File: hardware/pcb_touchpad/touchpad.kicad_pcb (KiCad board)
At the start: 2 copper layers, 23 parts

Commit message: drew outline of trackpad
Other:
- board outline added: 41.3 x 30.3 mm

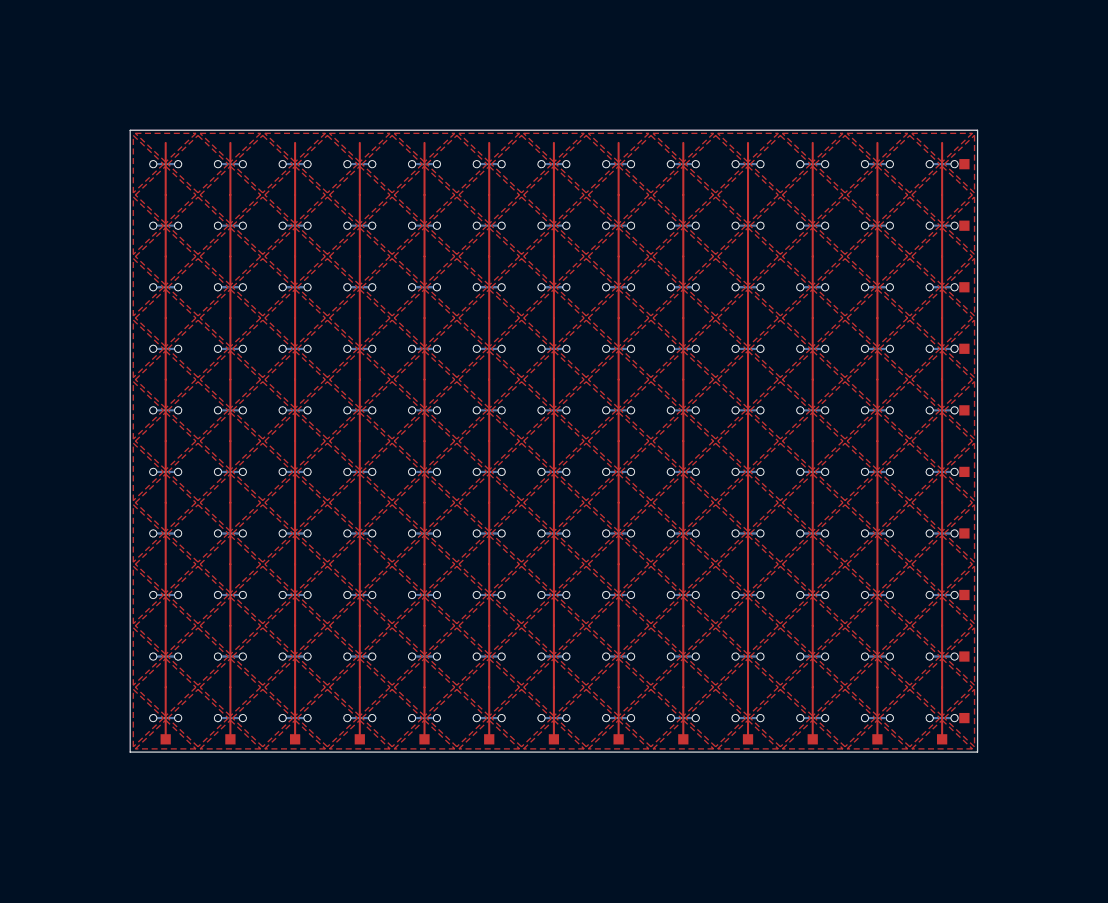
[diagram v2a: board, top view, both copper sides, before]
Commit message: modified QFN footprint of IQS9151
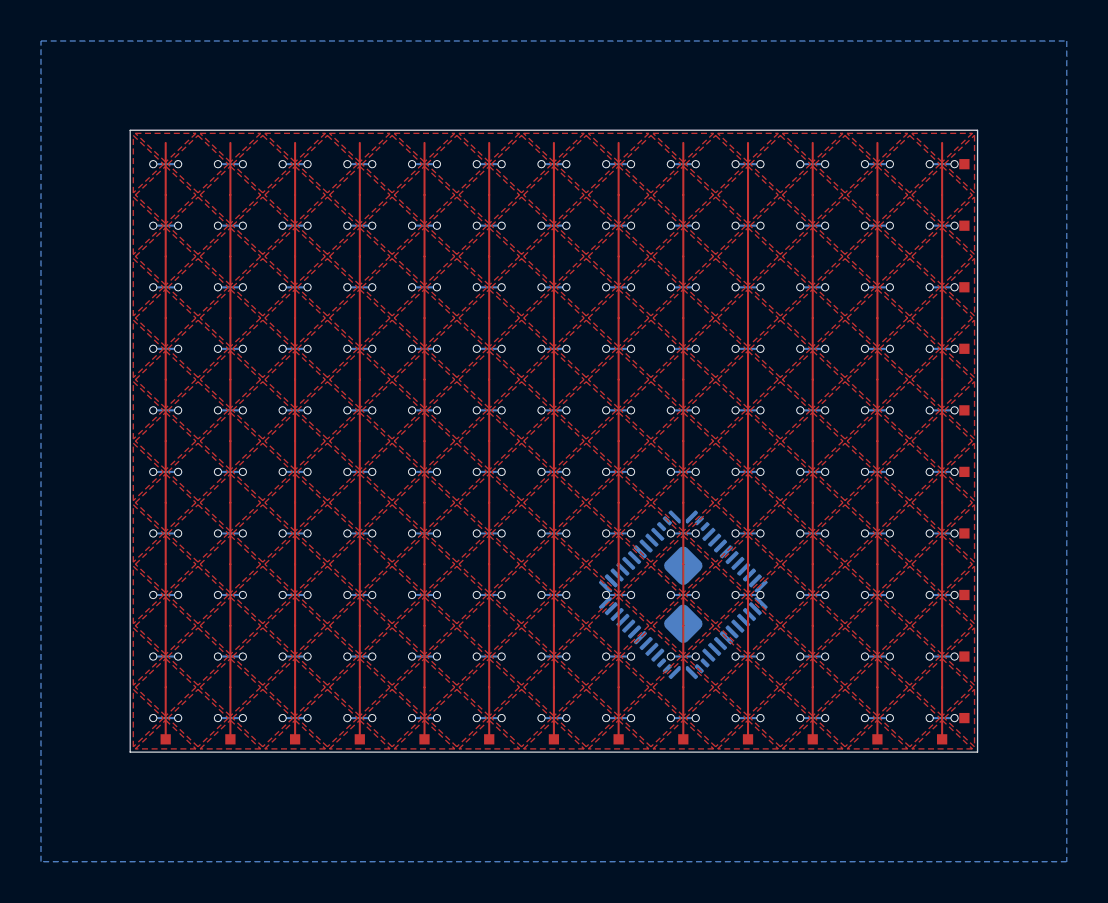
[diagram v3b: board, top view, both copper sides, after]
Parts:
- added U1: IQS9151, Package_DFN_QFN:VQFN-52-1EP_6x6mm_P0.4mm_EP4.7x4.7mm, B.Cu at (169.8, 92.0)
- COL1, COL10, COL2, COL3, COL4, COL5, COL6, COL7, COL8, COL9, ROW1, ROW10, ROW11, ROW12, ROW13, ROW2, ROW3, ROW4, ROW5, ROW6, ROW7, ROW8, ROW9: value (none) -> TESTPOINTPAD_0_5MM
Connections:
- COL1 pad P1: COL1 -> Net-(U1-RX9/TX9)
- COL10 pad P1: COL10 -> Net-(U1-RX0/TX0)
- COL2 pad P1: COL2 -> Net-(U1-RX8/TX8)
- COL3 pad P1: COL3 -> Net-(U1-RX7/TX7)
- COL4 pad P1: COL4 -> Net-(U1-RX6/TX6)
- COL5 pad P1: COL5 -> Net-(U1-RX5/TX5)
- COL6 pad P1: COL6 -> Net-(U1-RX4/TX4)
- COL7 pad P1: COL7 -> Net-(U1-RX3/TX3)
- COL8 pad P1: COL8 -> Net-(U1-RX2/TX2)
- COL9 pad P1: COL9 -> Net-(U1-RX1/TX1)
- ROW1 pad P1: ROW1 -> Net-(U1-TX43)
- ROW10 pad P1: ROW10 -> Net-(U1-TX34)
- ROW11 pad P1: ROW11 -> Net-(U1-TX33)
- ROW12 pad P1: ROW12 -> Net-(U1-RX12/TX12)
- ROW13 pad P1: ROW13 -> Net-(U1-RX11/TX11)
- ROW2 pad P1: ROW2 -> Net-(U1-TX42)
- ROW3 pad P1: ROW3 -> Net-(U1-TX41)
- ROW4 pad P1: ROW4 -> Net-(U1-TX40)
- ROW5 pad P1: ROW5 -> Net-(U1-TX39)
- ROW6 pad P1: ROW6 -> Net-(U1-TX38)
- ROW7 pad P1: ROW7 -> Net-(U1-TX37)
- ROW8 pad P1: ROW8 -> Net-(U1-TX36)
- ROW9 pad P1: ROW9 -> Net-(U1-TX35)
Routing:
- net (no net): track 0.00 -> 141.8 mm, vias 0 -> 234
- net Net-(U1-TX33): track 0.00 -> 31.5 mm, vias 0 -> 4
- net Net-(U1-TX40): track 0.00 -> 30.3 mm, vias 0 -> 2
- net ROW5: track 29.1 -> 0.00 mm
- net Net-(U1-TX39): track 0.00 -> 29.1 mm
- net ROW12: track 29.1 -> 0.00 mm
- net ROW10: track 29.1 -> 0.00 mm
- net Net-(U1-TX34): track 0.00 -> 29.1 mm
- net Net-(U1-RX12/TX12): track 0.00 -> 29.1 mm
- net ROW9: track 29.1 -> 0.00 mm
- net ROW7: track 29.1 -> 0.00 mm
- net ROW11: track 29.1 -> 0.00 mm
- net Net-(U1-TX37): track 0.00 -> 29.1 mm
- net Net-(U1-TX35): track 0.00 -> 29.1 mm
- net ROW8: track 29.1 -> 0.00 mm
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- added copper zone on B.Cu, net GND
- added copper zone on F.Cu, net Net-(U1-RX0/TX0)
- added copper zone on F.Cu, net Net-(U1-RX11/TX11)
- added copper zone on F.Cu, net Net-(U1-RX12/TX12)
- added copper zone on F.Cu, net Net-(U1-RX1/TX1)
- added copper zone on F.Cu, net Net-(U1-RX2/TX2)
- added copper zone on F.Cu, net Net-(U1-RX3/TX3)
- added copper zone on F.Cu, net Net-(U1-RX4/TX4)
- added copper zone on F.Cu, net Net-(U1-RX5/TX5)
- added copper zone on F.Cu, net Net-(U1-RX6/TX6)
- added copper zone on F.Cu, net Net-(U1-RX7/TX7)
- added copper zone on F.Cu, net Net-(U1-RX8/TX8)
- added copper zone on F.Cu, net Net-(U1-RX9/TX9)
- added copper zone on F.Cu, net Net-(U1-TX33)
- added copper zone on F.Cu, net Net-(U1-TX34)
- added copper zone on F.Cu, net Net-(U1-TX35)
- added copper zone on F.Cu, net Net-(U1-TX36)
- added copper zone on F.Cu, net Net-(U1-TX37)
- added copper zone on F.Cu, net Net-(U1-TX38)
- added copper zone on F.Cu, net Net-(U1-TX39)
- added copper zone on F.Cu, net Net-(U1-TX40)
- added copper zone on F.Cu, net Net-(U1-TX41)
- added copper zone on F.Cu, net Net-(U1-TX42)
- added copper zone on F.Cu, net Net-(U1-TX43)
- removed copper zone on F.Cu, net COL1
- removed copper zone on F.Cu, net COL10
- removed copper zone on F.Cu, net COL2
- removed copper zone on F.Cu, net COL3
- removed copper zone on F.Cu, net COL4
- removed copper zone on F.Cu, net COL5
- removed copper zone on F.Cu, net COL6
- removed copper zone on F.Cu, net COL7
- removed copper zone on F.Cu, net COL8
- removed copper zone on F.Cu, net COL9
- removed copper zone on F.Cu, net ROW1
- removed copper zone on F.Cu, net ROW10
- removed copper zone on F.Cu, net ROW11
- removed copper zone on F.Cu, net ROW12
- removed copper zone on F.Cu, net ROW13
- removed copper zone on F.Cu, net ROW2
- removed copper zone on F.Cu, net ROW3
- removed copper zone on F.Cu, net ROW4
- removed copper zone on F.Cu, net ROW5
- removed copper zone on F.Cu, net ROW6
- removed copper zone on F.Cu, net ROW7
- removed copper zone on F.Cu, net ROW8
- removed copper zone on F.Cu, net ROW9
